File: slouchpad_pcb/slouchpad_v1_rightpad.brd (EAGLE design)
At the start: 41 x 69 mm, 10 parts

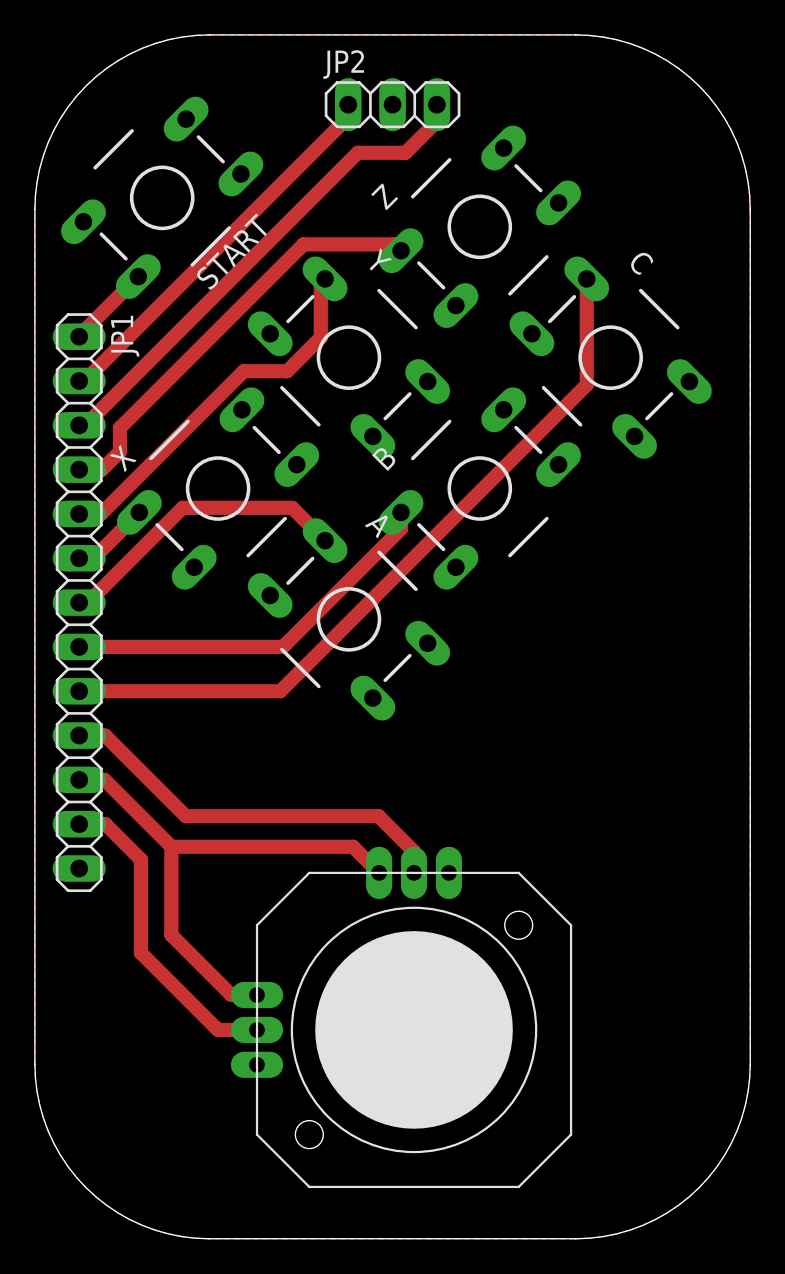
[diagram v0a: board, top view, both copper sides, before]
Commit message: Retooled the project to be a modular joypad
Rather than being a shield for the SparkFun Pro Micro Arduino, the slouchpad will simply be a modular joypad for use with any microcontroller.

Modified the license to reflect the removal of the SparkFun Pro Micro

Removed backup design files

Created button layout for left thumb pad

Modified all board positions to units of mm where possible.

Signed-off-by: Eric Jones <eric.r.k.jones@gmail.com>
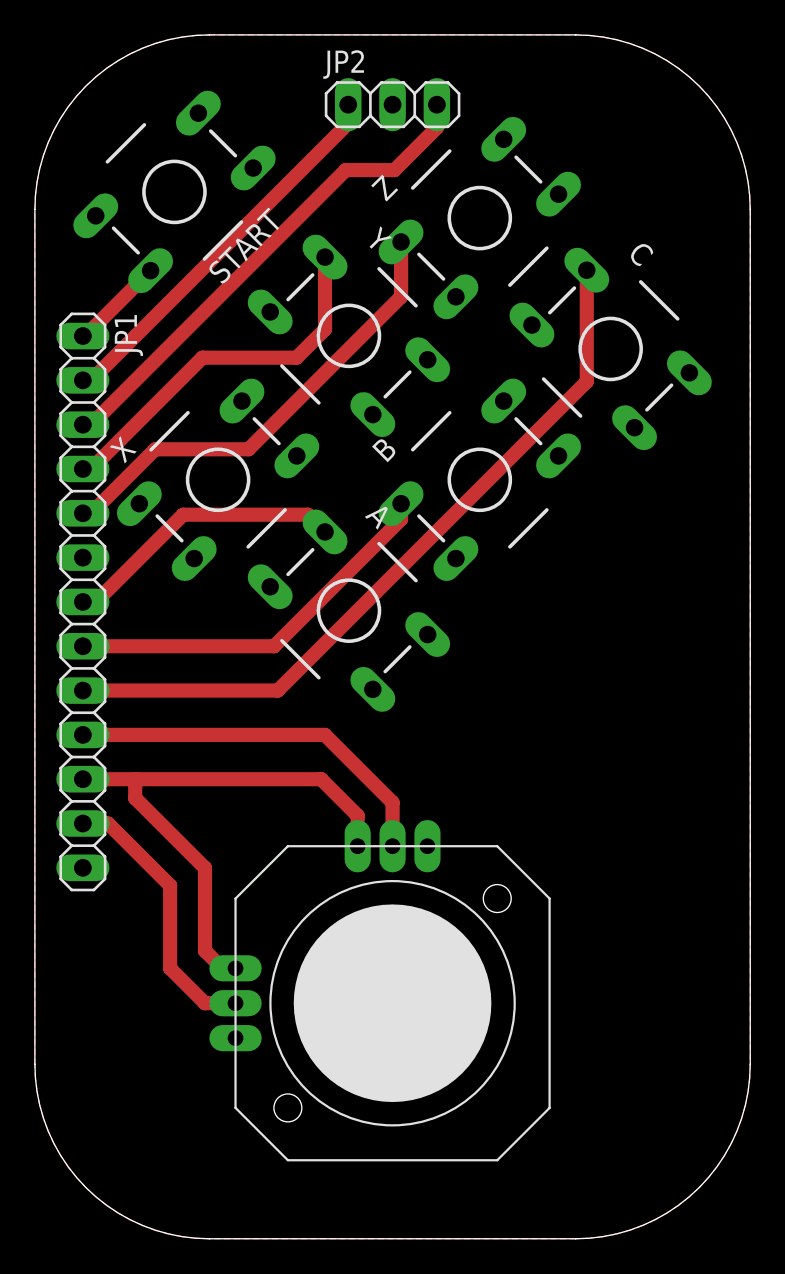
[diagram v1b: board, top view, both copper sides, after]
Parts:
- moved JOY1 1.96 mm to (20.5, 13.5)
- moved Y 1.25 mm to (18.0, 51.8)
- moved START 0.78 mm to (8.00, 60.0)
- moved A 0.50 mm to (18.0, 36.0)
- moved B 0.50 mm to (25.5, 43.5)
- moved C 0.50 mm to (33.0, 51.0)
- moved X 0.50 mm to (10.5, 43.5)
- moved Z 0.50 mm to (25.5, 58.5)
- moved JP1 0.21 mm to (2.75, 36.5)
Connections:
- net Y: now also JP1.4; no longer JP1.5
- net Z: now also JP1.5; no longer JP1.4
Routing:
- net X: track 4.54 -> 0.15 mm
- net JOYX: track 18.2 -> 15.8 mm
- net Z: track 25.1 -> 26.5 mm
- net JOYY: track 23.2 -> 21.9 mm
- net VCC: track 30.8 -> 32.0 mm
- net N$2: track 22.4 -> 23.2 mm
- net A: track 17.1 -> 16.4 mm
- net START: track 4.85 -> 5.43 mm

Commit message: Finished board layouts
Cleaned up schematics
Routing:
- net X: track 0.15 -> 4.75 mm
- net B: track 22.1 -> 24.8 mm
- net C: track 42.6 -> 44.6 mm
- net VCC: track 32.0 -> 31.0 mm
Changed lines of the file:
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@@
 <layer number="43" name="vRestrict" color="2" fill="10" visible="yes" active="yes"/>
 <layer number="44" name="Drills" color="7" fill="1" visible="no" active="yes"/>
-<layer number="45" name="Holes" color="7" fill="1" visible="no" active="yes"/>
+<layer number="45" name="Holes" color="7" fill="1" visible="yes" active="yes"/>
 <layer number="46" name="Milling" color="3" fill="1" visible="no" active="yes"/>
 <layer number="47" name="Measures" color="7" fill="1" visible="no" active="yes"/>
@@
 <wire x1="41" y1="10" x2="41" y2="59" width="0" layer="20"/>
 <wire x1="41" y1="59" x2="31" y2="69" width="0" layer="20" curve="90"/>
+<hole x="8" y="7" drill="3.2"/>
+<hole x="33" y="7" drill="3.2"/>
+<hole x="33" y="34.5" drill="3.2"/>
+<hole x="8" y="34.5" drill="3.2"/>
 </plain>
 <attributes>
@@
 <contactref element="JOY1" pad="X+"/>
 <contactref element="JP1" pad="11"/>
-<wire x1="2.75" y1="26.34" x2="5.75" y2="26.34" width="0.8128" layer="1"/>
-<wire x1="5.75" y1="26.34" x2="5.75" y2="25.25" width="0.8128" layer="1"/>
-<wire x1="9.75" y1="21.25" x2="5.75" y2="25.25" width="0.8128" layer="1"/>
-<wire x1="9.75" y1="16.5" x2="9.75" y2="21.25" width="0.8128" layer="1"/>
 <wire x1="9.75" y1="16.5" x2="10.75" y2="15.5" width="0.8128" layer="1"/>
 <wire x1="10.75" y1="15.5" x2="11.5" y2="15.5" width="0.8128" layer="1"/>
-<wire x1="16.41" y1="26.34" x2="18.5" y2="24.25" width="0.8128" layer="1"/>
-<wire x1="18.5" y1="24.25" x2="18.5" y2="22.5" width="0.8128" layer="1"/>
-<wire x1="5.75" y1="26.34" x2="16.41" y2="26.34" width="0.8128" layer="1"/>
+<wire x1="2.75" y1="26.34" x2="3.66" y2="26.34" width="0.8128" layer="1"/>
+<wire x1="9.75" y1="20.25" x2="9.75" y2="16.5" width="0.8128" layer="1"/>
+<wire x1="5.375" y1="24.625" x2="3.66" y2="26.34" width="0.8128" layer="1"/>
+<wire x1="5.375" y1="24.625" x2="9.75" y2="20.25" width="0.8128" layer="1"/>
+<wire x1="18.5" y1="22.5" x2="18.5" y2="24.25" width="0.8128" layer="1"/>
+<wire x1="18.5" y1="24.25" x2="17.5" y2="25.25" width="0.8128" layer="1"/>
+<wire x1="17.5" y1="25.25" x2="6" y2="25.25" width="0.8128" layer="1"/>
+<wire x1="6" y1="25.25" x2="5.375" y2="24.625" width="0.8128" layer="1"/>
 </signal>
 <signal name="JOYX">
 <contactref element="JOY1" pad="X"/>
 <contactref element="JP1" pad="12"/>
-<wire x1="2.75" y1="23.8" x2="4.2" y2="23.8" width="0.8128" layer="1"/>
-<wire x1="7.75" y1="20.25" x2="7.75" y2="15.5" width="0.8128" layer="1"/>
-<wire x1="4.2" y1="23.8" x2="7.75" y2="20.25" width="0.8128" layer="1"/>
 <wire x1="7.75" y1="15.5" x2="9.75" y2="13.5" width="0.8128" layer="1"/>
 <wire x1="9.75" y1="13.5" x2="11.5" y2="13.5" width="0.8128" layer="1"/>
+<wire x1="2.75" y1="23.8" x2="3.45" y2="23.8" width="0.8128" layer="1"/>
+<wire x1="7.75" y1="19.5" x2="7.75" y2="15.5" width="0.8128" layer="1"/>
+<wire x1="3.45" y1="23.8" x2="7.75" y2="19.5" width="0.8128" layer="1"/>
 </signal>
 <signal name="JOYY">
 <contactref element="JOY1" pad="Y"/>
 <contactref element="JP1" pad="10"/>
-<wire x1="20.5" y1="22.5" x2="20.5" y2="25" width="0.8128" layer="1"/>
-<wire x1="20.5" y1="25" x2="16.62" y2="28.88" width="0.8128" layer="1"/>
-<wire x1="16.62" y1="28.88" x2="2.75" y2="28.88" width="0.8128" layer="1"/>
+<wire x1="20.5" y1="25" x2="20.5" y2="22.5" width="0.8128" layer="1"/>
+<wire x1="2.75" y1="28.88" x2="3.62" y2="28.88" width="0.8128" layer="1"/>
+<wire x1="18.25" y1="27.25" x2="20.5" y2="25" width="0.8128" layer="1"/>
+<wire x1="3.62" y1="28.88" x2="5.25" y2="27.25" width="0.8128" layer="1"/>
+<wire x1="5.25" y1="27.25" x2="18.25" y2="27.25" width="0.8128" layer="1"/>
 </signal>
 <signal name="A">
@@
 <contactref element="B" pad="2"/>
 <contactref element="JP1" pad="8"/>
-<wire x1="2.75" y1="33.96" x2="13.71" y2="33.96" width="0.8128" layer="1"/>
 <wire x1="20.98741875" y1="41.23741875" x2="20.98741875" y2="42.130509375" width="0.8128" layer="1"/>
-<wire x1="13.71" y1="33.96" x2="20.98741875" y2="41.23741875" width="0.8128" layer="1"/>
+<wire x1="2.75" y1="33.96" x2="3.29" y2="33.96" width="0.8128" layer="1"/>
+<wire x1="3.29" y1="33.96" x2="6.5" y2="30.75" width="0.8128" layer="1"/>
+<wire x1="6.5" y1="30.75" x2="10.5" y2="30.75" width="0.8128" layer="1"/>
+<wire x1="10.5" y1="30.75" x2="20.98741875" y2="41.23741875" width="0.8128" layer="1"/>
 <wire x1="20.98741875" y1="42.130509375" x2="26.8694875" y2="48.012578125" width="0" layer="19" extent="1-1"/>
 </signal>
@@
 <contactref element="C" pad="2"/>
 <contactref element="JP1" pad="9"/>
-<wire x1="2.75" y1="31.42" x2="13.92" y2="31.42" width="0.8128" layer="1"/>
 <wire x1="31.630509375" y1="49.130509375" x2="31.630509375" y2="55.512578125" width="0.8128" layer="1"/>
-<wire x1="13.92" y1="31.42" x2="31.630509375" y2="49.130509375" width="0.8128" layer="1"/>
+<wire x1="11.5" y1="29" x2="31.630509375" y2="49.130509375" width="0.8128" layer="1"/>
+<wire x1="2.75" y1="31.42" x2="3.33" y2="31.42" width="0.8128" layer="1"/>
+<wire x1="5.75" y1="29" x2="11.5" y2="29" width="0.8128" layer="1"/>
+<wire x1="3.33" y1="31.42" x2="5.75" y2="29" width="0.8128" layer="1"/>
 <wire x1="31.630509375" y1="49.130509375" x2="37.512578125" y2="49.630509375" width="0" layer="19" extent="1-1"/>
 </signal>
@@
 <contactref element="X" pad="2"/>
 <contactref element="JP1" pad="6"/>
-<wire x1="2.896909375" y1="39.04" x2="2.75" y2="39.04" width="0.8128" layer="1"/>
+<wire x1="2.75" y1="39.04" x2="3.29" y2="39.04" width="0.8128" layer="1"/>
+<wire x1="5.98741875" y1="41.73741875" x2="5.98741875" y2="42.130509375" width="0.8128" layer="1"/>
+<wire x1="3.29" y1="39.04" x2="5.98741875" y2="41.73741875" width="0.8128" layer="1"/>
 <wire x1="5.98741875" y1="42.130509375" x2="11.8694875" y2="48.012578125" width="0" layer="19" extent="1-1"/>
-<wire x1="2.896909375" y1="39.04" x2="5.98741875" y2="42.130509375" width="0" layer="19" extent="1-1"/>
 </signal>
 <signal name="Y">

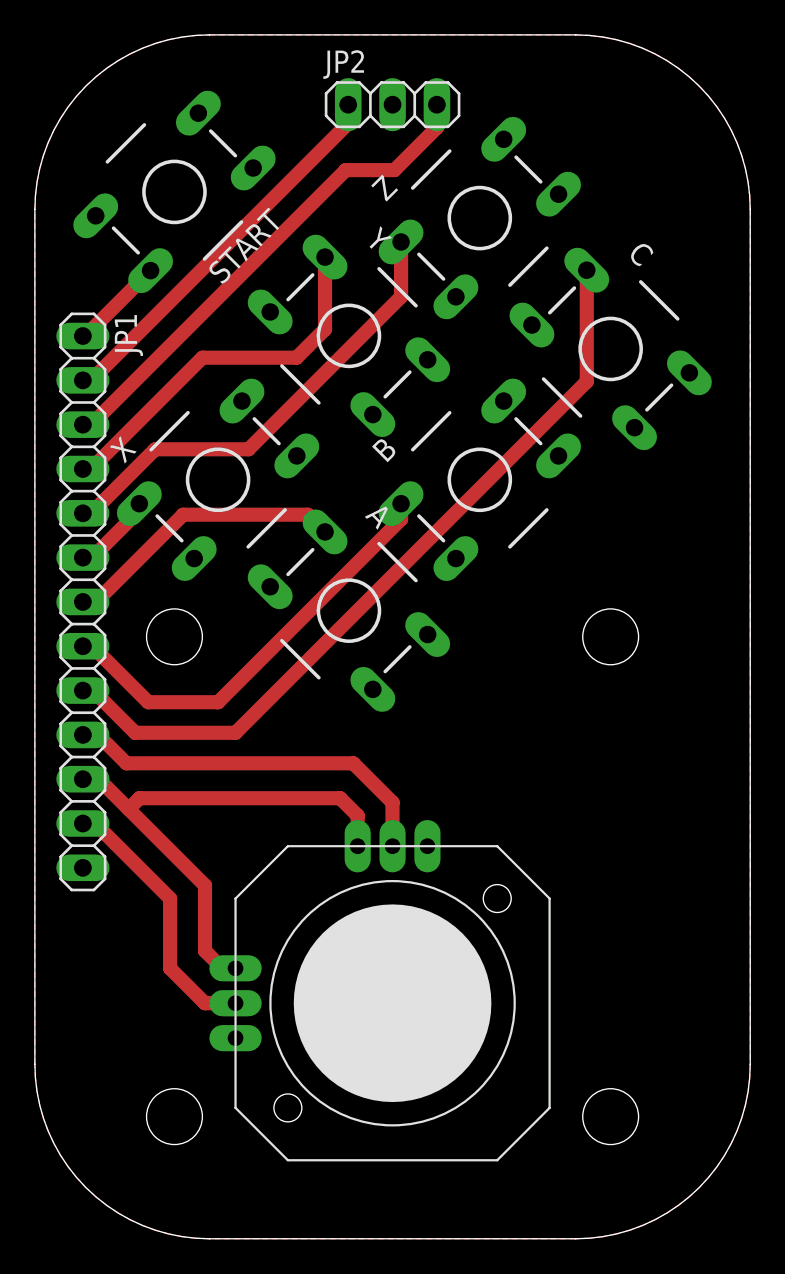
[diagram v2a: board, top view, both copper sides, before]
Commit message: Finished silkscreen of boards
Moved traces to bottom layer to represent design intention
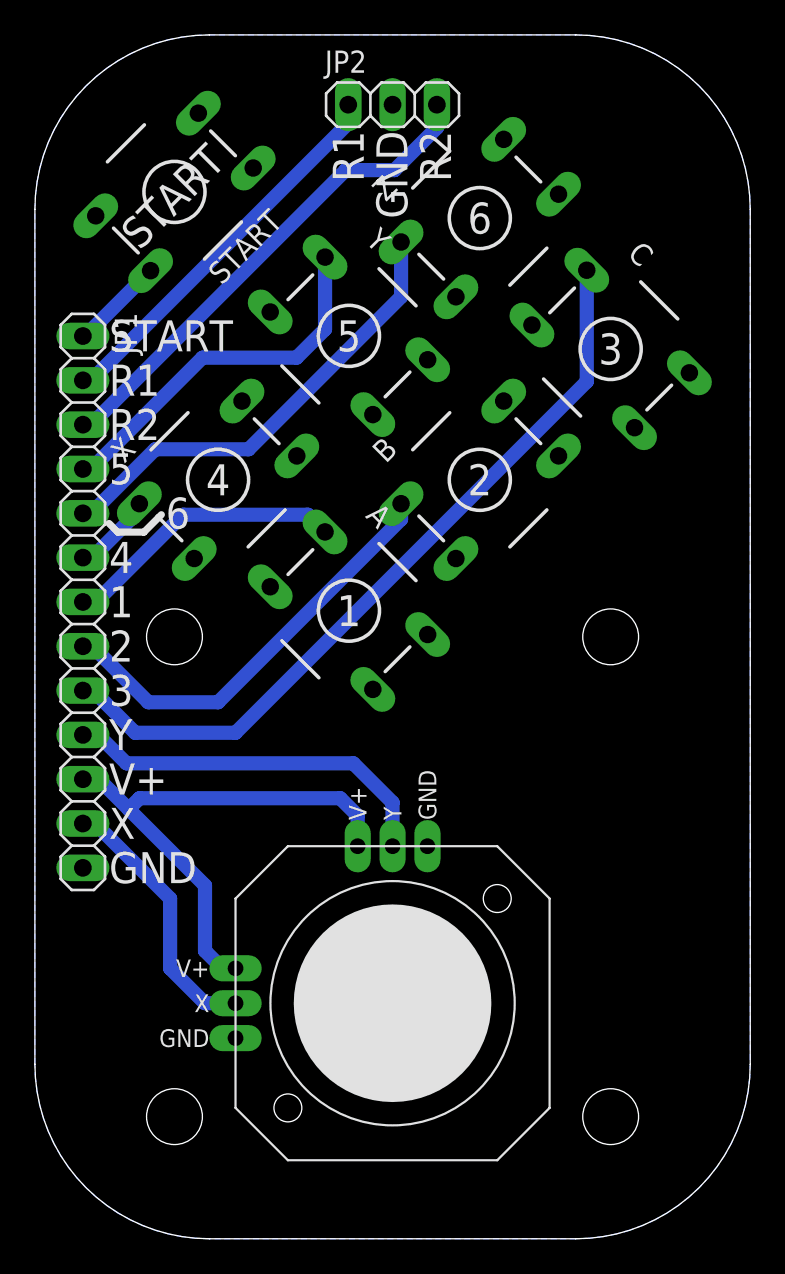
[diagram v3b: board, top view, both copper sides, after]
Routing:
- net N$2: track 23.2 -> 22.1 mm
- added copper zone on layer 16, net GND
- removed copper zone on layer 1, net GND
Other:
- board text added: "1"
- board text added: "2"
- board text added: "3"
- board text added: "4"
- board text added: "5"
- board text added: "6"
- board text added: "GND"
- board text added: "R1"
- board text added: "R2"
- board text added: "START"
- board text added: "V+"
- board text added: "X"
- board text added: "Y"

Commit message: Added dimensions to baord drawings and fixed button 5 position to have correct spacing.
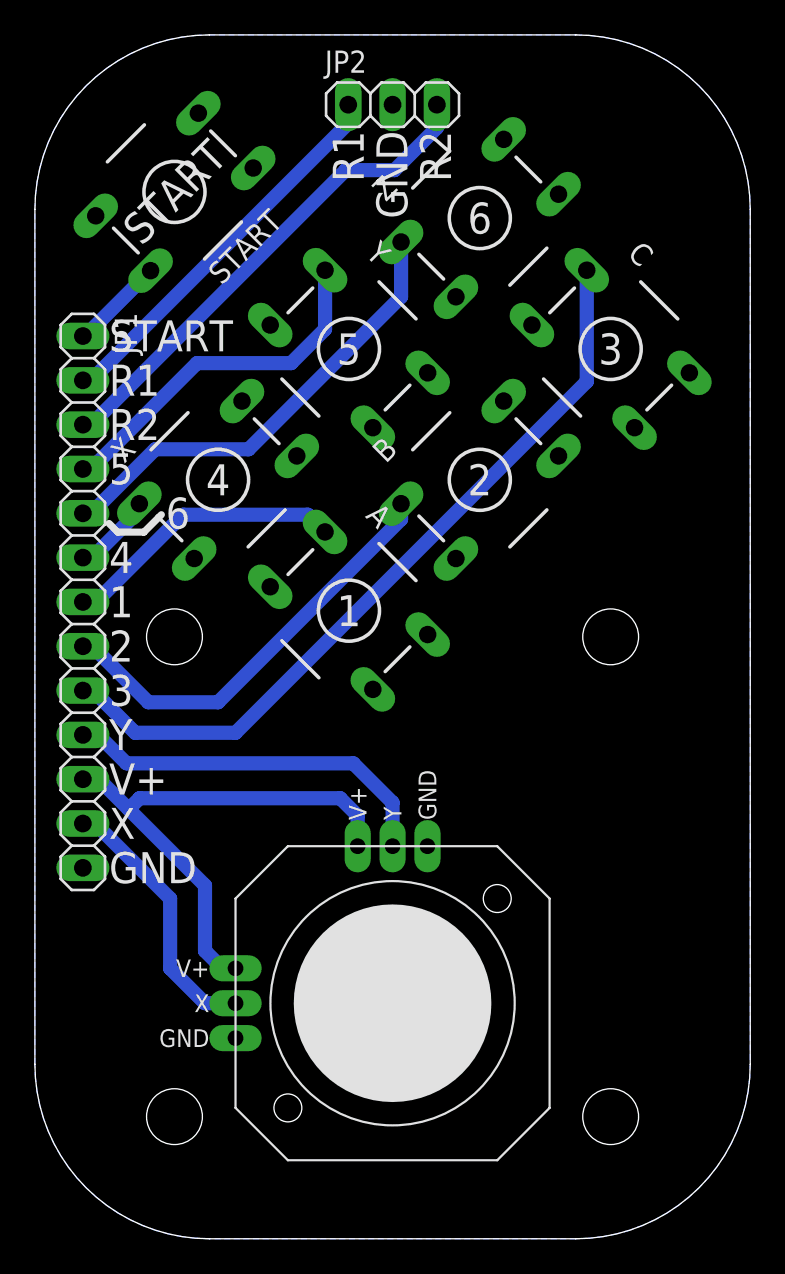
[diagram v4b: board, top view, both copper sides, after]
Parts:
- moved Y 0.75 mm to (18.0, 51.0)
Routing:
- net Y: track 21.3 -> 20.6 mm
